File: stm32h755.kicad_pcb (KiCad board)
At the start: 2 copper layers, 21 parts, among them U1 STM32H757IITx

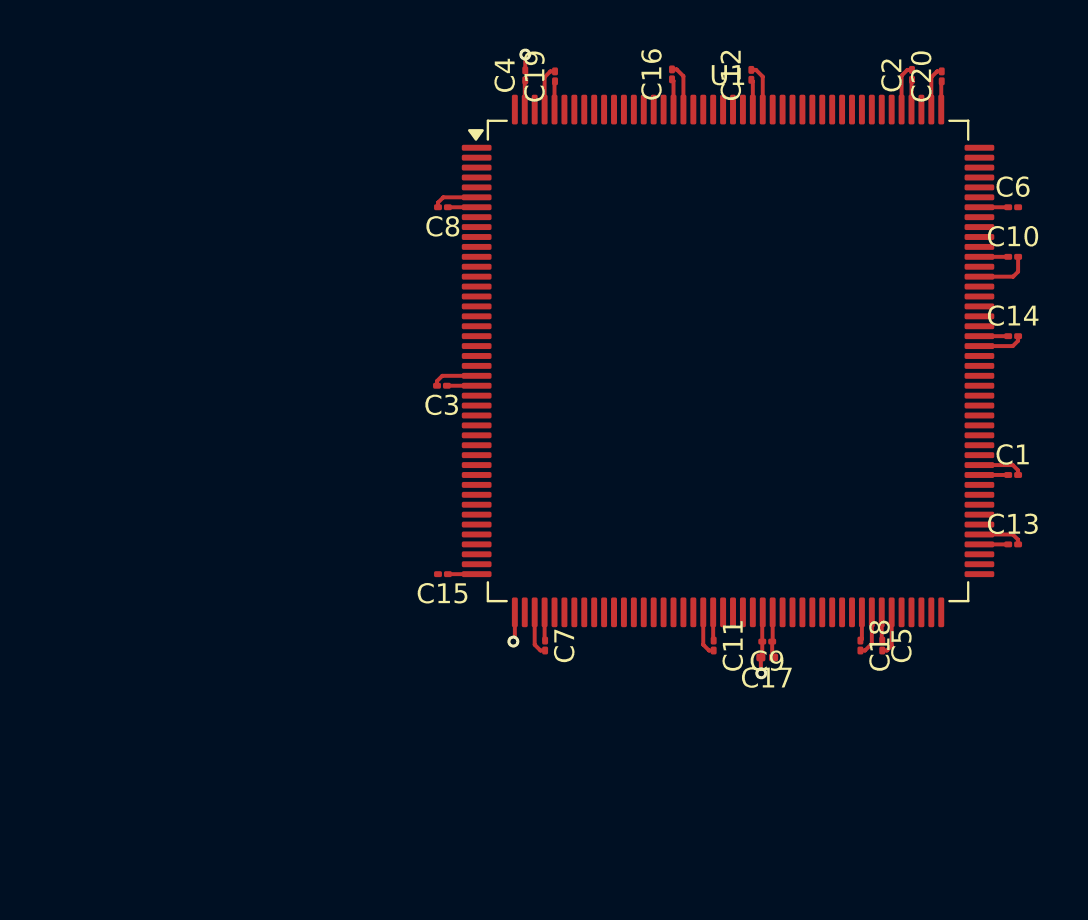
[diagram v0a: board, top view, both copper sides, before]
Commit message: Decoupling Capacitors Placed
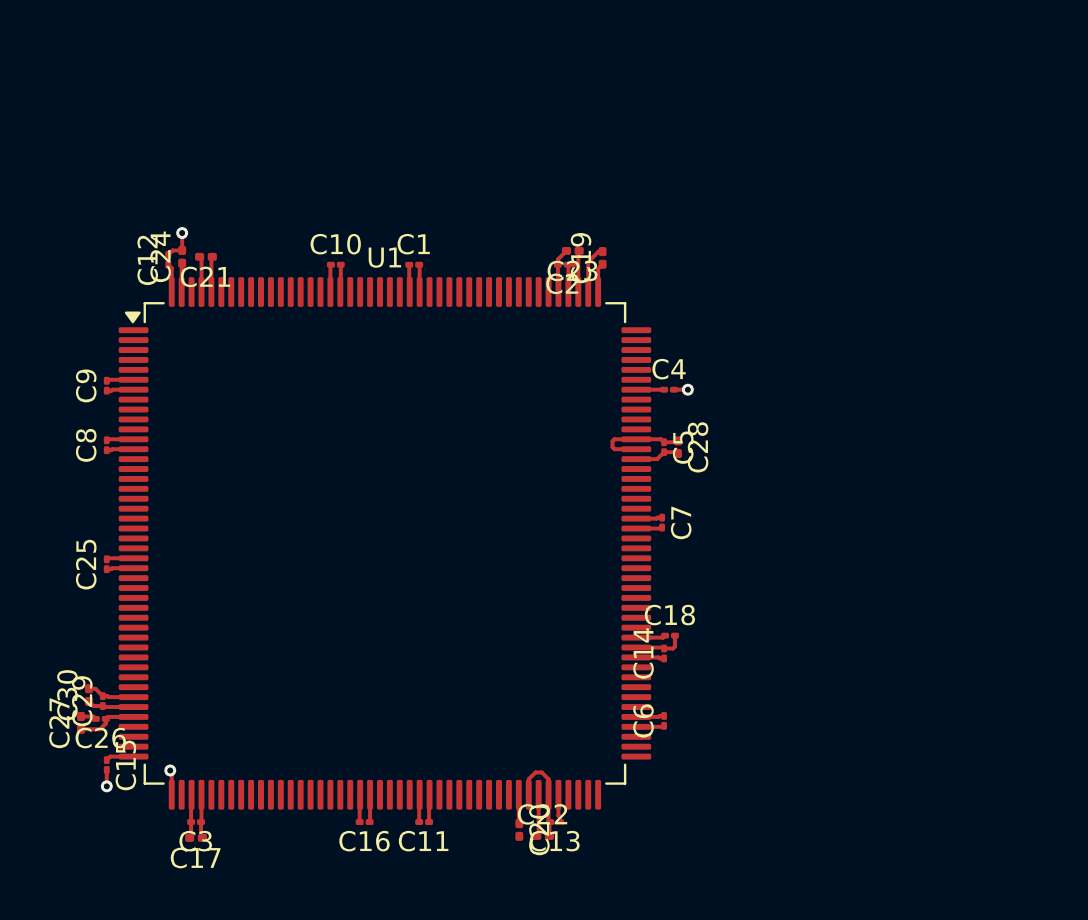
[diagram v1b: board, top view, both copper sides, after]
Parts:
- added C21: 2u2, Capacitor_SMD:C_0201_0603Metric, F.Cu at (101.5, 72.5)
- added C22: 4u7, Capacitor_SMD:C_0201_0603Metric, F.Cu at (118.5, 101.7)
- added C23: 4u7, Capacitor_SMD:C_0201_0603Metric, F.Cu at (120.0, 72.2)
- added C24: 4u7, Capacitor_SMD:C_0201_0603Metric, F.Cu at (100.3, 72.5)
- added C25: 100nF, Capacitor_SMD:C_01005_0402Metric, F.Cu at (96.5, 88.0)
- added C26: 100nF, Capacitor_SMD:C_01005_0402Metric, F.Cu at (96.2, 95.8)
- added C27: 1uF, Capacitor_SMD:C_0201_0603Metric, F.Cu at (95.2, 96.0)
- added C28: 1uF, Capacitor_SMD:C_0201_0603Metric, F.Cu at (125.3, 82.1)
- added C29: 100nF, Capacitor_SMD:C_01005_0402Metric, F.Cu at (96.3, 94.9)
- added C30: 1uF, Capacitor_SMD:C_0201_0603Metric, F.Cu at (95.6, 94.6)
- C19, C20: footprint Capacitor_SMD:C_01005_0402Metric -> Capacitor_SMD:C_0201_0603Metric
- moved C20 43.6 mm to (117.3, 101.4), turned to -90 degrees
- moved C16 40.8 mm to (109.5, 101.0), turned to 180 degrees
- moved C9 35.7 mm to (96.5, 79.0), turned to 90 degrees
- moved C10 34.2 mm to (108.0, 72.9)
- moved C1 32.0 mm to (112.0, 72.9)
- moved C6 31.3 mm to (124.6, 95.9), turned to 90 degrees
- moved C12 30.8 mm to (99.6, 72.7)
- moved C17 30.2 mm to (101.0, 101.8)
- moved C13 27.0 mm to (119.1, 101.0), turned to 180 degrees
- moved C3 25.3 mm to (101.0, 101.0)
- moved C14 23.8 mm to (124.6, 92.5), turned to 90 degrees
- moved C8 20.8 mm to (96.5, 82.0), turned to 90 degrees
- moved C2 20.0 mm to (119.5, 72.9), turned to 180 degrees
- moved U1 19.6 mm to (110.5, 87.0)
- moved C15 19.5 mm to (96.5, 98.1), turned to -90 degrees
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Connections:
- U1 pad 101: unconnected-(U1-VCAPDSI-Pad101) -> VCAP
- U1 pad 120: unconnected-(U1-VDD50_USB-Pad120) -> +3V3
- U1 pad 39: unconnected-(U1-VREF+-Pad39) -> /VREF
- U1 pad 40: unconnected-(U1-VDDA-Pad40) -> +3.3VA
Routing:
- net +3V3: track 24.4 -> 34.2 mm
- net +3.3VA: track 0.00 -> 3.04 mm
- net /VREF: track 0.00 -> 2.37 mm
- net GND: track 40.7 -> 38.6 mm, vias 3 -> 4
- net VCAP: track 4.33 -> 6.24 mm

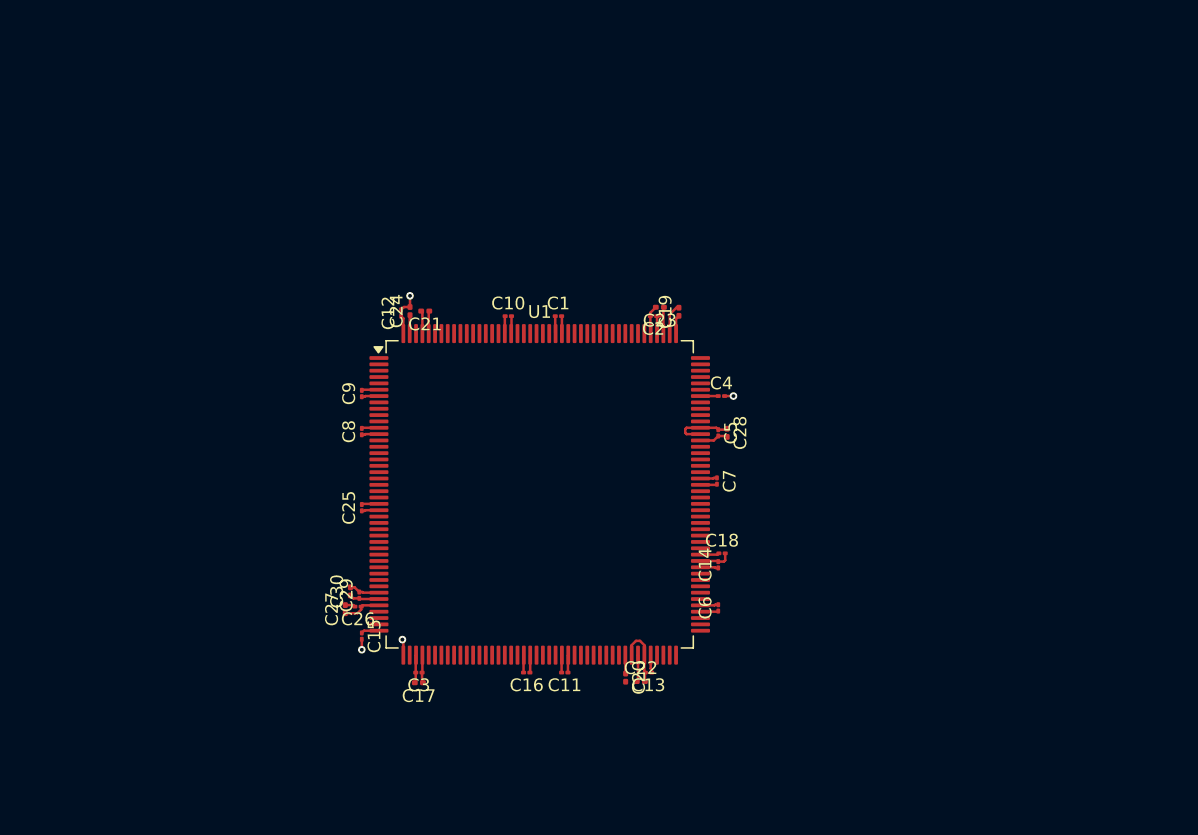
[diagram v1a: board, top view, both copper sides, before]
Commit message: Decoupling Capacitors Placed
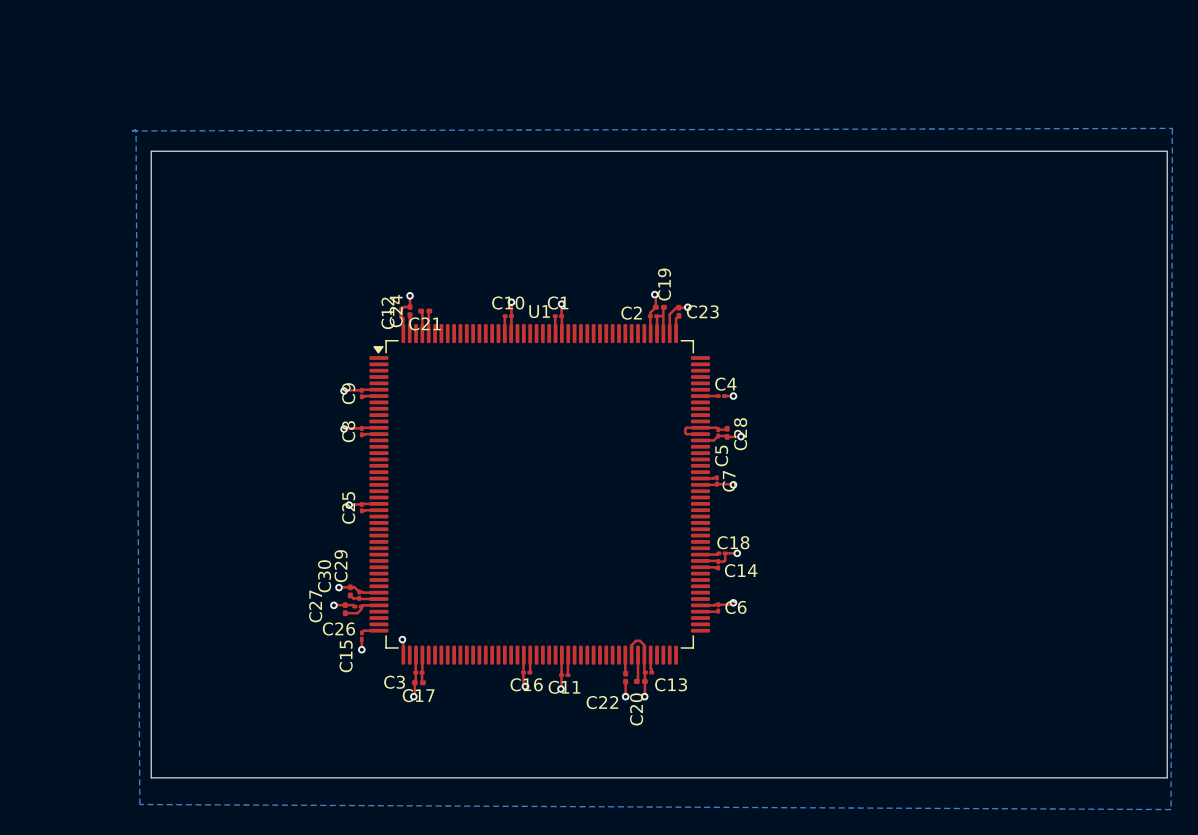
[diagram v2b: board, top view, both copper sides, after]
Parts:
- moved C11 0.20 mm to (112.5, 101.2)
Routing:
- net GND: track 38.6 -> 58.8 mm, vias 4 -> 22
- added copper zone on B.Cu, net GND
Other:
- board outline added: 80.1 x 49.4 mm

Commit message: Redesigned PCB
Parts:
- added C31: 10uF, Capacitor_SMD:C_0603_1608Metric, F.Cu at (86.4, 98.8)
- added C32: 10uF, Capacitor_SMD:C_0603_1608Metric, F.Cu at (83.3, 98.6)
- added U2: AMS1117, Package_TO_SOT_SMD:SOT-223-3_TabPin2, F.Cu at (85.5, 104.7)
- moved C14 46.2 mm to (87.8, 64.5)
- moved C20 45.9 mm to (90.1, 64.5), turned to 90 degrees
- moved C13 43.8 mm to (84.5, 74.2)
- moved C7 42.7 mm to (84.5, 71.2), turned to 180 degrees
- moved C11 40.2 mm to (96.1, 64.5), turned to 90 degrees
- moved C17 39.7 mm to (86.7, 64.8)
- moved C22 38.5 mm to (108.6, 64.5), turned to 90 degrees
- moved C16 37.6 mm to (100.1, 64.6), turned to 90 degrees
- moved C6 35.1 mm to (89.6, 93.2), turned to -90 degrees
- moved C1 32.2 mm to (84.5, 89.7), turned to 180 degrees
- moved C2 27.5 mm to (101.1, 93.3), turned to -90 degrees
- moved C19 26.2 mm to (105.6, 93.4), turned to -90 degrees
- moved C23 25.1 mm to (106.6, 93.4), turned to -90 degrees
- moved C25 21.6 mm to (113.2, 74.2), turned to 0 degrees
- moved C9 16.7 mm to (113.2, 77.7), turned to 0 degrees
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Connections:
- C1 pad 1: +3V3 -> +3.3VA
- C10 pad 1: +3V3 -> +3.3VA
- C11 pad 1: +3V3 -> +3.3VA
- C12 pad 1: +3V3 -> +3.3VA
- C13 pad 1: +3V3 -> +3.3VA
- C14 pad 1: +3V3 -> +3.3VA
- C15 pad 1: +3V3 -> +3.3VA
- C16 pad 1: +3V3 -> +3.3VA
- C17 pad 1: +3V3 -> +3.3VA
- C2 pad 1: +3V3 -> +3.3VA
- C22 pad 1: +3V3 -> +3.3VA
- C23 pad 1: +3V3 -> +3.3VA
- C24 pad 1: +3V3 -> +3.3VA
- C25 pad 1: +3V3 -> +3.3VA
- C28 pad 1: +3V3 -> +3.3VA
- C29 pad 1: /VREF -> +3.3VA
- C3 pad 1: +3V3 -> +3.3VA
- C30 pad 1: /VREF -> +3.3VA
- C4 pad 1: +3V3 -> +3.3VA
- C5 pad 1: +3V3 -> +3.3VA
- C6 pad 1: +3V3 -> +3.3VA
- C7 pad 1: +3V3 -> +3.3VA
- C8 pad 1: +3V3 -> +3.3VA
- C9 pad 1: +3V3 -> +3.3VA
- U1 pad 113: +3V3 -> +3.3VA
- U1 pad 120: +3V3 -> +3.3VA
- U1 pad 121: +3V3 -> +3.3VA
- U1 pad 126: +3V3 -> +3.3VA
- U1 pad 13: +3V3 -> +3.3VA
- U1 pad 135: +3V3 -> +3.3VA
- U1 pad 136: +3V3 -> +3.3VA
- U1 pad 152: +3V3 -> +3.3VA
- U1 pad 160: +3V3 -> +3.3VA
- U1 pad 175: +3V3 -> +3.3VA
- U1 pad 176: +3V3 -> +3.3VA
- U1 pad 25: +3V3 -> +3.3VA
- U1 pad 39: /VREF -> +3.3VA
- U1 pad 44: +3V3 -> +3.3VA
- U1 pad 48: +3V3 -> +3.3VA
- U1 pad 65: +3V3 -> +3.3VA
- U1 pad 7: +3V3 -> +3.3VA
- U1 pad 71: +3V3 -> +3.3VA
- U1 pad 82: +3V3 -> +3.3VA
- U1 pad 84: +3V3 -> +3.3VA
- U1 pad 92: +3V3 -> +3.3VA
- U1 pad 99: +3V3 -> +3.3VA
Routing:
- net +3.3VA: track 3.04 -> 79.0 mm, vias 0 -> 28
- net +3V3: track 34.2 -> 0.00 mm
- net GND: track 58.8 -> 72.5 mm, vias 22 -> 40
- net /VREF: track 2.37 -> 0.00 mm
- net /VIN: track 0.00 -> 2.19 mm
- added copper zone on B.Cu, net +3.3VA
- added copper zone on F.Cu, net +3.3VA
- added copper zone on F.Cu, net GND
- added copper zone on In1.Cu, net GND
- added copper zone on In2.Cu, net GND
- removed copper zone on B.Cu, net GND
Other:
- board size 80.1 x 49.4 mm -> 60 x 60 mm
- copper layers 2 -> 4

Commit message: Redesigned PCB
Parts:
- moved C31 0.09 mm to (86.4, 98.8)
- moved C32 0.09 mm to (83.3, 98.5)
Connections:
- net +3.3VA renamed +3V3
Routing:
- net +3V3: track 79.0 -> 89.5 mm, vias 28 -> 35

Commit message: Redesigned PCB
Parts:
- added D1: LED, LED_SMD:LED_0201_0603Metric, F.Cu at (90.4, 96.7)
- added J1: Conn_01x04_Pin, Connector_PinHeader_2.54mm:PinHeader_1x04_P2.54mm_Horizontal, F.Cu at (119.0, 59.3)
- added J2: Conn_01x04_Pin, Connector_PinHeader_2.54mm:PinHeader_1x04_P2.54mm_Horizontal, F.Cu at (102.8, 98.3)
- added J3: Conn_01x04_Pin, Connector_PinHeader_2.54mm:PinHeader_1x04_P2.54mm_Horizontal, F.Cu at (118.4, 91.7)
- added J4: Conn_01x04_Pin, Connector_PinHeader_2.54mm:PinHeader_1x04_P2.54mm_Horizontal, F.Cu at (76.9, 60.7)
- added J5: Conn_01x08_Pin, Connector_PinHeader_2.54mm:PinHeader_1x08_P2.54mm_Vertical, F.Cu at (113.2, 54.7)
- added J6: Conn_01x02_Pin, Connector_PinHeader_2.54mm:PinHeader_1x02_P2.54mm_Vertical, F.Cu at (73.5, 96.6)
- added R1: 10K, Resistor_SMD:R_0201_0603Metric, F.Cu at (88.9, 96.3)
- added R2: R, Resistor_SMD:R_0201_0603Metric, F.Cu at (92.0, 64.4)
- moved U2 2.45 mm to (85.2, 102.3)
- moved C31 2.45 mm to (86.1, 96.4)
- moved C32 2.45 mm to (83.0, 96.1)
- moved C1 0.14 mm to (84.4, 89.8)
- moved C11 0.14 mm to (96.0, 64.6)
- moved C12 0.14 mm to (113.1, 71.3)
- moved C16 0.14 mm to (100.0, 64.7)
- moved C18 0.14 mm to (113.0, 83.8)
- moved C20 0.14 mm to (90.0, 64.6)
- moved C22 0.14 mm to (108.5, 64.6)
- moved C24 0.14 mm to (88.5, 64.5)
- moved C25 0.14 mm to (113.0, 74.3)
- moved C27 0.14 mm to (84.3, 88.8)
- moved C28 0.14 mm to (113.1, 73.6)
- moved C30 0.14 mm to (84.3, 87.3)
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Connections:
- net /VIN renamed +5V
- C18 pad 1: VCAP -> Net-(U1-VCAPDSI)
- C19 pad 1: VCAP -> Net-(C19-Pad1)
- C20 pad 1: VCAP -> Net-(C20-Pad1)
- C21 pad 1: VCAP -> Net-(C21-Pad1)
- C29 pad 1: +3V3 -> /VREF
- C30 pad 1: +3V3 -> /VREF
- U1 pad 101: VCAP -> Net-(U1-VCAPDSI)
- U1 pad 132: unconnected-(U1-PA13-Pad132) -> Net-(J1-Pin_3)
- U1 pad 133: VCAP -> Net-(C21-Pad1)
- U1 pad 138: unconnected-(U1-PA14-Pad138) -> Net-(J1-Pin_2)
- U1 pad 143: unconnected-(U1-PD0-Pad143) -> Net-(J5-Pin_1)
- U1 pad 144: unconnected-(U1-PD1-Pad144) -> Net-(J5-Pin_2)
- U1 pad 145: unconnected-(U1-PD2-Pad145) -> Net-(J5-Pin_3)
- U1 pad 146: unconnected-(U1-PD3-Pad146) -> Net-(J5-Pin_4)
- U1 pad 147: unconnected-(U1-PD4-Pad147) -> Net-(J5-Pin_5)
- U1 pad 148: unconnected-(U1-PD5-Pad148) -> Net-(J5-Pin_6)
- U1 pad 149: unconnected-(U1-PD6-Pad149) -> Net-(J5-Pin_7)
- U1 pad 150: unconnected-(U1-PD7-Pad150) -> Net-(J5-Pin_8)
- U1 pad 165: unconnected-(U1-PB6-Pad165) -> Net-(J4-Pin_3)
- U1 pad 166: unconnected-(U1-PB7-Pad166) -> Net-(J4-Pin_2)
- U1 pad 167: unconnected-(U1-BOOT0-Pad167) -> Net-(U1-BOOT0)
- U1 pad 172: VCAP -> Net-(C20-Pad1)
- U1 pad 39: +3V3 -> /VREF
- U1 pad 43: unconnected-(U1-PA2-Pad43) -> Net-(J2-Pin_3)
- U1 pad 46: unconnected-(U1-PA3-Pad46) -> Net-(J2-Pin_2)
- U1 pad 80: VCAP -> Net-(C19-Pad1)
- U1 pad 87: unconnected-(U1-PB14-Pad87) -> Net-(J3-Pin_3)
- U1 pad 88: unconnected-(U1-PB15-Pad88) -> Net-(J3-Pin_2)
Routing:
- net +3V3: track 89.5 -> 270.7 mm, vias 35 -> 4
- net GND: track 72.5 -> 40.2 mm, vias 40 -> 0
- net Net-(J2-Pin_3): track 0.00 -> 26.5 mm, vias 0 -> 2
- net Net-(J5-Pin_1): track 0.00 -> 17.9 mm
- net Net-(J4-Pin_2): track 0.00 -> 17.1 mm
- net Net-(J2-Pin_2): track 0.00 -> 16.7 mm
- net Net-(J1-Pin_2): track 0.00 -> 16.2 mm
- net Net-(J4-Pin_3): track 0.00 -> 15.6 mm
- net Net-(J5-Pin_2): track 0.00 -> 14.5 mm
- net Net-(J5-Pin_8): track 0.00 -> 14.0 mm
- net Net-(J5-Pin_3): track 0.00 -> 13.6 mm
- net Net-(J3-Pin_3): track 0.00 -> 13.2 mm
- net Net-(J5-Pin_7): track 0.00 -> 13.1 mm
- net Net-(J5-Pin_4): track 0.00 -> 12.9 mm
- net Net-(J5-Pin_6): track 0.00 -> 12.3 mm
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- added copper zone on B.Cu, net GND
- removed copper zone on B.Cu, net +3V3
- removed copper zone on F.Cu, net +3V3
- removed copper zone on In1.Cu, net GND
- removed copper zone on In2.Cu, net GND
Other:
- copper layers 4 -> 2
- board text added: "3V3"
- board text added: "GND"
- board text added: "RX"
- board text added: "SCL"
- board text added: "SDA"
- board text added: "SWCLK"
- board text added: "SWDIO"
- board text added: "TX"
- board text added: "VIN"

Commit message: Redesigned PCB
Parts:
- renumbered J4 to I2C1, J6 to PWR, J1 to SWD, J3 to UART1, J2 to UART2
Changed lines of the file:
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@@
 		(descr "Through hole straight pin header, 1x02, 2.54mm pitch, single row")
 		(tags "Through hole pin header THT 1x02 2.54mm single row")
-		(property "Reference" "J6"
+		(property "Reference" "PWR"
 			(at 0 -2.38 0)
 			(layer "F.SilkS")
@@
 		(descr "Through hole angled pin header, 1x04, 2.54mm pitch, 6mm pin length, single row")
 		(tags "Through hole angled pin header THT 1x04 2.54mm single row")
-		(property "Reference" "J2"
-			(at 4.385 -2.27 90)
+		(property "Reference" "UART2"
+			(at 2.755 -2.73 90)
 			(layer "F.SilkS")
 			(effects
@@
 		(descr "Through hole angled pin header, 1x04, 2.54mm pitch, 6mm pin length, single row")
 		(tags "Through hole angled pin header THT 1x04 2.54mm single row")
-		(property "Reference" "J1"
+		(property "Reference" "SWD"
 			(at 2.75 -2.64 0)
 			(layer "F.SilkS")
@@
 		(descr "Through hole angled pin header, 1x04, 2.54mm pitch, 6mm pin length, single row")
 		(tags "Through hole angled pin header THT 1x04 2.54mm single row")
-		(property "Reference" "J4"
+		(property "Reference" "I2C1"
 			(at 4.385 -2.27 90)
 			(layer "F.SilkS")
@@
 		(descr "Through hole angled pin header, 1x04, 2.54mm pitch, 6mm pin length, single row")
 		(tags "Through hole angled pin header THT 1x04 2.54mm single row")
-		(property "Reference" "J3"
+		(property "Reference" "UART1"
 			(at 4.04 -3.05 0)
 			(layer "F.SilkS")
